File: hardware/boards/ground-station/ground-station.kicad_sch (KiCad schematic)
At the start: 2 parts, among them J101 Raspberry_Pi_2_3, J102 Conn_01x15

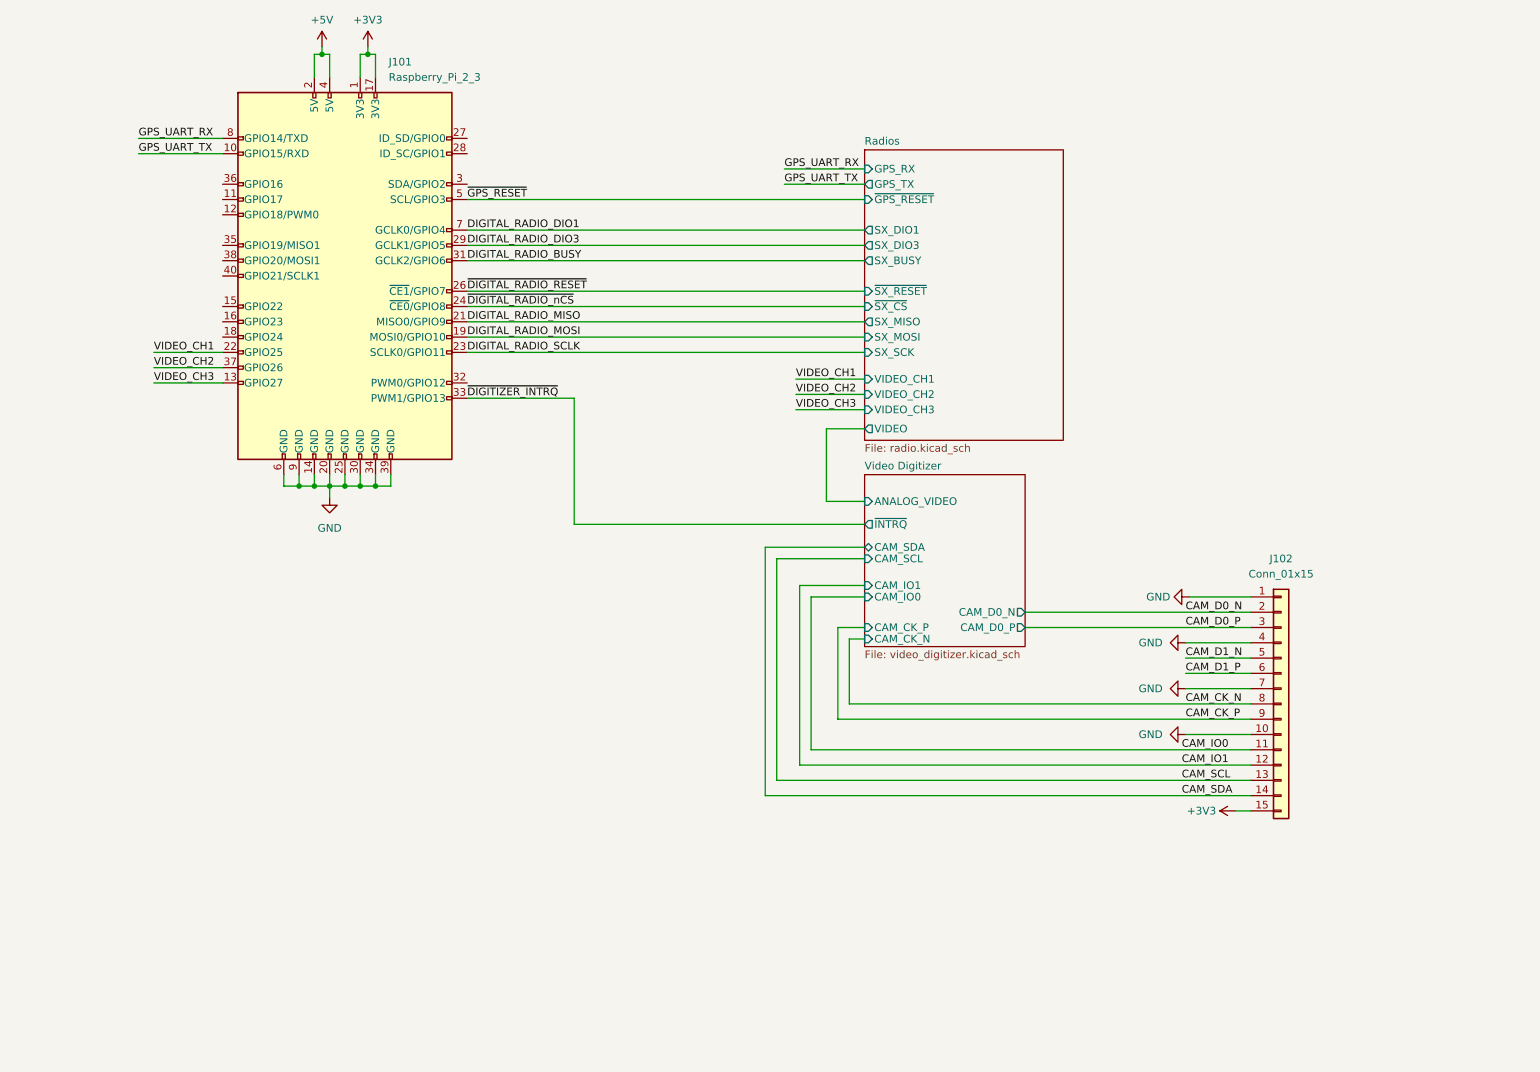
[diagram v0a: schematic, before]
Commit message: Added power supplies to digitizer IC
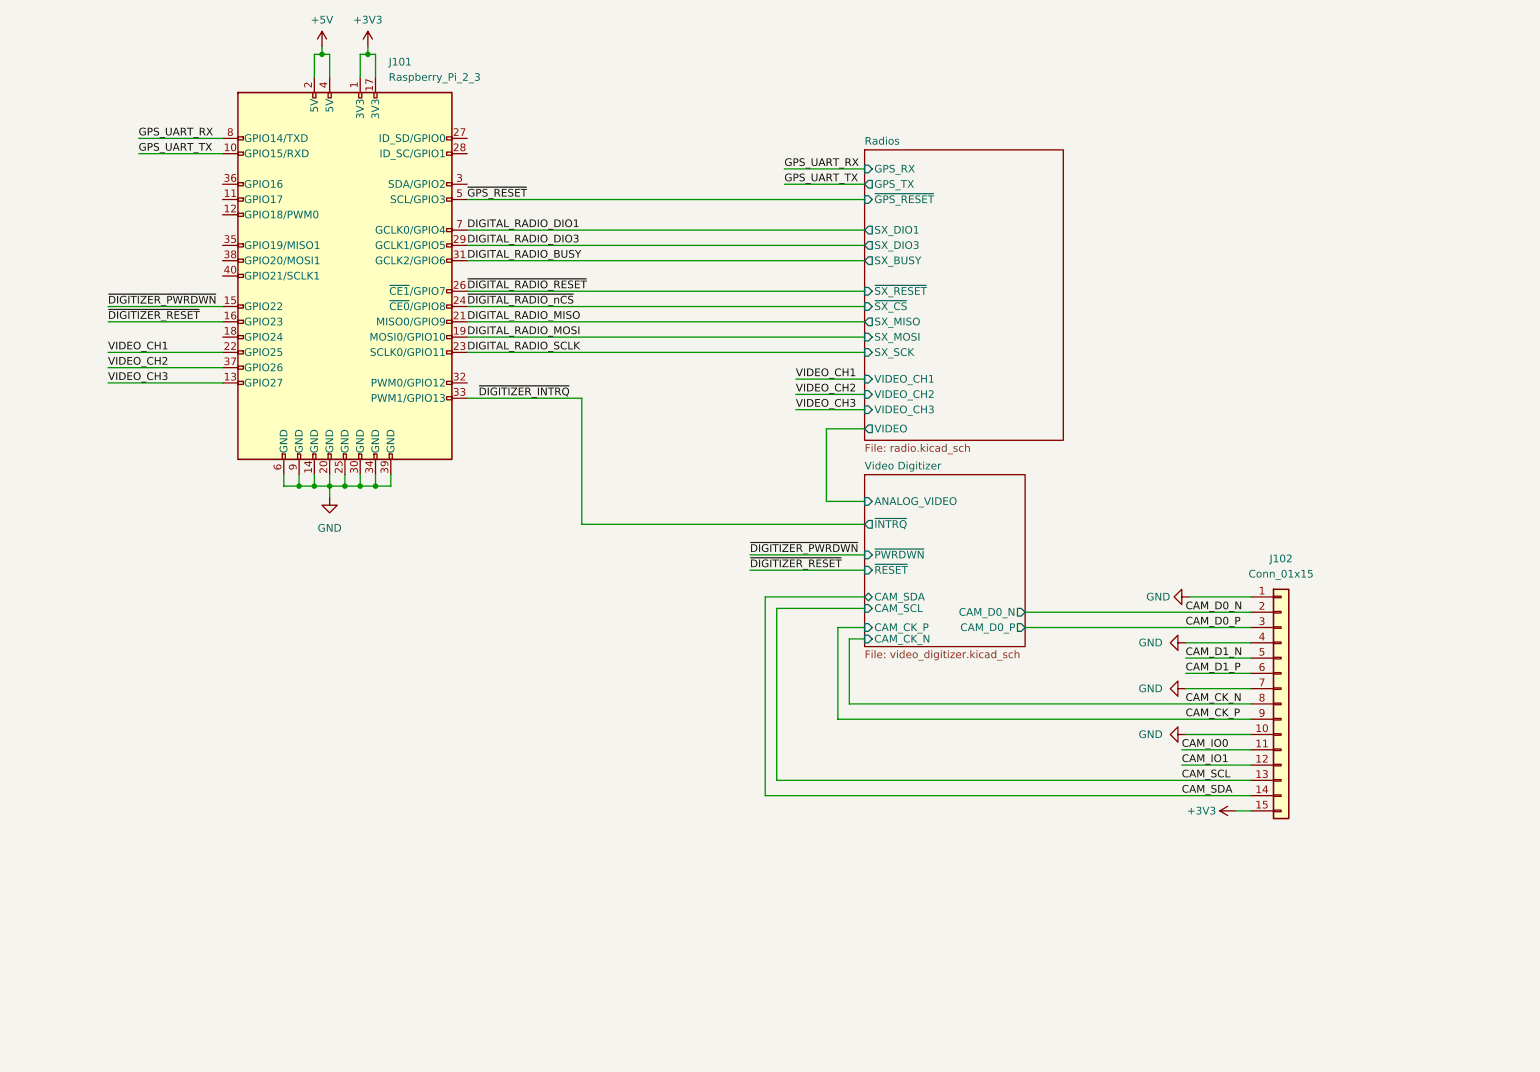
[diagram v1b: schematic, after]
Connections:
- net ~{DIGITIZER_PWRDWN}: now reaches J101.15 (GPIO22)
- net ~{DIGITIZER_RESET}: now reaches J101.16 (GPIO23)
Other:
- sheet Video Digitizer ports: added ~{PWRDWN}, ~{RESET}; removed CAM_IO0, CAM_IO1
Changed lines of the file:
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@@
+    (stroke (width 0) (type default))
+  )
+  (wire (pts (xy 223.52 135.255) (xy 234.95 135.255))
     (stroke (width 0) (type default))
   )
@@
     (stroke (width 0) (type default))
   )
+  (wire (pts (xy 45.085 64.135) (xy 64.135 64.135))
+    (stroke (width 0) (type default))
+  )
+  (wire (pts (xy 45.085 74.295) (xy 64.135 74.295))
+    (stroke (width 0) (type default))
+  )
   (wire (pts (xy 76.835 89.535) (xy 76.835 91.44))
     (stroke (width 0) (type default))
@@
     (stroke (width 0) (type default))
   )
-  (wire (pts (xy 52.705 71.755) (xy 64.135 71.755))
+  (wire (pts (xy 45.085 69.215) (xy 64.135 69.215))
     (stroke (width 0) (type default))
   )
@@
     (stroke (width 0) (type default))
   )
-  (wire (pts (xy 160.02 137.795) (xy 234.95 137.795))
-    (stroke (width 0) (type default))
-  )
   (wire (pts (xy 79.375 23.495) (xy 79.375 19.685))
     (stroke (width 0) (type default))
@@
     (stroke (width 0) (type default))
   )
-  (wire (pts (xy 122.555 97.79) (xy 122.555 76.835))
-    (stroke (width 0) (type default))
-  )
-  (wire (pts (xy 161.925 109.855) (xy 161.925 135.255))
+  (wire (pts (xy 123.825 97.79) (xy 123.825 76.835))
     (stroke (width 0) (type default))
   )
@@
     (stroke (width 0) (type default))
   )
-  (wire (pts (xy 170.815 103.505) (xy 156.21 103.505))
+  (wire (pts (xy 170.815 111.76) (xy 156.21 111.76))
     (stroke (width 0) (type default))
   )
@@
     (stroke (width 0) (type default))
   )
-  (wire (pts (xy 170.815 109.855) (xy 161.925 109.855))
-    (stroke (width 0) (type default))
-  )
-  (wire (pts (xy 161.925 135.255) (xy 234.95 135.255))
+  (wire (pts (xy 45.085 71.755) (xy 64.135 71.755))
+    (stroke (width 0) (type default))
+  )
+  (wire (pts (xy 45.085 61.595) (xy 64.135 61.595))
     (stroke (width 0) (type default))
   )
@@
     (stroke (width 0) (type default))
   )
-  (wire (pts (xy 52.705 74.295) (xy 64.135 74.295))
+  (wire (pts (xy 223.52 137.795) (xy 234.95 137.795))
     (stroke (width 0) (type default))
   )
@@
     (stroke (width 0) (type default))
   )
-  (wire (pts (xy 160.02 107.95) (xy 160.02 137.795))
-    (stroke (width 0) (type default))
-  )
   (wire (pts (xy 89.535 19.685) (xy 88.265 19.685))
     (stroke (width 0) (type default))
@@
     (stroke (width 0) (type default))
   )
+  (wire (pts (xy 151.765 105.41) (xy 170.815 105.41))
+    (stroke (width 0) (type default))
+  )
   (wire (pts (xy 84.455 91.44) (xy 81.915 91.44))
     (stroke (width 0) (type default))
@@
     (stroke (width 0) (type default))
   )
-  (wire (pts (xy 122.555 76.835) (xy 104.775 76.835))
+  (wire (pts (xy 104.775 76.835) (xy 123.825 76.835))
     (stroke (width 0) (type default))
   )
@@
     (stroke (width 0) (type default))
   )
-  (wire (pts (xy 156.21 103.505) (xy 156.21 140.335))
-    (stroke (width 0) (type default))
-  )
-  (wire (pts (xy 170.815 101.6) (xy 154.305 101.6))
+  (wire (pts (xy 156.21 111.76) (xy 156.21 140.335))
+    (stroke (width 0) (type default))
+  )
+  (wire (pts (xy 170.815 109.855) (xy 154.305 109.855))
     (stroke (width 0) (type default))
   )
@@
     (stroke (width 0) (type default))
   )
-  (wire (pts (xy 154.305 101.6) (xy 154.305 142.875))
-    (stroke (width 0) (type default))
-  )
-  (wire (pts (xy 170.815 107.95) (xy 160.02 107.95))
+  (wire (pts (xy 154.305 109.855) (xy 154.305 142.875))
     (stroke (width 0) (type default))
   )
@@
     (stroke (width 0) (type default))
   )
-  (wire (pts (xy 170.815 97.79) (xy 122.555 97.79))
-    (stroke (width 0) (type default))
-  )
-  (wire (pts (xy 52.705 69.215) (xy 64.135 69.215))
+  (wire (pts (xy 170.815 97.79) (xy 123.825 97.79))
     (stroke (width 0) (type default))
   )
@@
     (stroke (width 0) (type default))
   )
+  (wire (pts (xy 151.765 102.87) (xy 170.815 102.87))
+    (stroke (width 0) (type default))
+  )
   (wire (pts (xy 104.775 69.215) (xy 170.815 69.215))
     (stroke (width 0) (type default))
@@
     (effects (font (size 1.27 1.27)) (justify left bottom))
   )
-  (label "VIDEO_CH3" (at 52.705 74.295 0) (fields_autoplaced)
+  (label "VIDEO_CH3" (at 45.085 74.295 0) (fields_autoplaced)
+    (effects (font (size 1.27 1.27)) (justify left bottom))
+  )
+  (label "~{DIGITIZER_PWRDWN}" (at 151.765 102.87 0) (fields_autoplaced)
     (effects (font (size 1.27 1.27)) (justify left bottom))
   )
@@
     (effects (font (size 1.27 1.27)) (justify left bottom))
   )
-  (label "VIDEO_CH2" (at 52.705 71.755 0) (fields_autoplaced)
+  (label "VIDEO_CH2" (at 45.085 71.755 0) (fields_autoplaced)
+    (effects (font (size 1.27 1.27)) (justify left bottom))
+  )
+  (label "~{DIGITIZER_RESET}" (at 45.085 64.135 0) (fields_autoplaced)
     (effects (font (size 1.27 1.27)) (justify left bottom))
   )
@@
     (effects (font (size 1.27 1.27)) (justify left bottom))
   )
-  (label "VIDEO_CH1" (at 52.705 69.215 0) (fields_autoplaced)
+  (label "VIDEO_CH1" (at 45.085 69.215 0) (fields_autoplaced)
     (effects (font (size 1.27 1.27)) (justify left bottom))
   )
@@
     (effects (font (size 1.27 1.27)) (justify left bottom))
   )
+  (label "~{DIGITIZER_PWRDWN}" (at 45.085 61.595 0) (fields_autoplaced)
+    (effects (font (size 1.27 1.27)) (justify left bottom))
+  )
   (label "CAM_SCL" (at 223.52 140.335 0) (fields_autoplaced)
     (effects (font (size 1.27 1.27)) (justify left bottom))
@@
     (effects (font (size 1.27 1.27)) (justify left bottom))
   )
-  (label "~{DIGITIZER_INTRQ}" (at 104.775 76.835 0) (fields_autoplaced)
+  (label "~{DIGITIZER_INTRQ}" (at 106.68 76.835 0) (fields_autoplaced)
     (effects (font (size 1.27 1.27)) (justify left bottom))
   )
@@
   )
   (label "CAM_D1_N" (at 224.155 120.015 0) (fields_autoplaced)
+    (effects (font (size 1.27 1.27)) (justify left bottom))
+  )
+  (label "~{DIGITIZER_RESET}" (at 151.765 105.41 0) (fields_autoplaced)
     (effects (font (size 1.27 1.27)) (justify left bottom))
   )
@@
       (effects (font (size 1.27 1.27)) (justify left))
     )
-    (pin "CAM_IO0" input (at 170.815 109.855 180)
-      (effects (font (size 1.27 1.27)) (justify left))
-    )
-    (pin "CAM_IO1" input (at 170.815 107.95 180)
-      (effects (font (size 1.27 1.27)) (justify left))
-    )
-    (pin "CAM_SCL" input (at 170.815 103.505 180)
-      (effects (font (size 1.27 1.27)) (justify left))
-    )
-    (pin "CAM_SDA" bidirectional (at 170.815 101.6 180)
+    (pin "CAM_SCL" input (at 170.815 111.76 180)
+      (effects (font (size 1.27 1.27)) (justify left))
+    )
+    (pin "CAM_SDA" bidirectional (at 170.815 109.855 180)
       (effects (font (size 1.27 1.27)) (justify left))
     )
@@
       (effects (font (size 1.27 1.27)) (justify left))
     )
+    (pin "~{PWRDWN}" input (at 170.815 102.87 180)
+      (effects (font (size 1.27 1.27)) (justify left))
+    )
+    (pin "~{RESET}" input (at 170.815 105.41 180)
+      (effects (font (size 1.27 1.27)) (justify left))
+    )

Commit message: transmitter tx stuff
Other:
- added sheet Power (Power.kicad_sch)
- added sheet Wireless Power TX (WirelessPowerTX.kicad_sch)
- note added: "NEED THESE I2C PINS MOVE IO SOMEWHERE"
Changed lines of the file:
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@@
     (stroke (width 0) (type default))
+  )
+  (text "NEED THESE I2C PINS\nMOVE IO SOMEWHERE\n" (at 116.84 40.64 0)
+    (effects (font (size 1.27 1.27)) (justify left bottom))
   )
   (label "CAM_D0_N" (at 224.155 112.395 0) (fields_autoplaced)
@@
     )
   )
+  (sheet (at 101.6 146.05) (size 46.99 38.1) (fields_autoplaced)
+    (stroke (width 0.1524) (type solid))
+    (fill (color 0 0 0 0.0000))
+    (property "Sheetname" "Wireless Power TX" (at 101.6 145.3384 0)
+      (effects (font (size 1.27 1.27)) (justify left bottom))
+    )
+    (property "Sheetfile" "WirelessPowerTX.kicad_sch" (at 101.6 184.7346 0)
+      (effects (font (size 1.27 1.27)) (justify left top))
+    )
+    (instances
+      (project "ground-station"
+        (path "/ce329892-de08-4d39-b253-15f3aaf1c085" (page "7"))
+      )
+    )
+  )
   (sheet (at 170.815 35.56) (size 33.02 48.26) (fields_autoplaced)
     (stroke (width 0.1524) (type solid))
@@
       )
     )
+  )
+  (sheet (at 29.21 102.87) (size 39.37 35.56) (fields_autoplaced)
+    (stroke (width 0.1524) (type solid))
+    (fill (color 0 0 0 0.0000))
+    (property "Sheetname" "Power" (at 29.21 102.1584 0)
+      (effects (font (size 1.27 1.27)) (justify left bottom))
+    )
+    (property "Sheetfile" "Power.kicad_sch" (at 29.21 139.0146 0)
+      (effects (font (size 1.27 1.27)) (justify left top))
+    )
+    (instances
+      (project "ground-station"
+        (path "/ce329892-de08-4d39-b253-15f3aaf1c085" (page "8"))
+      )
+    )

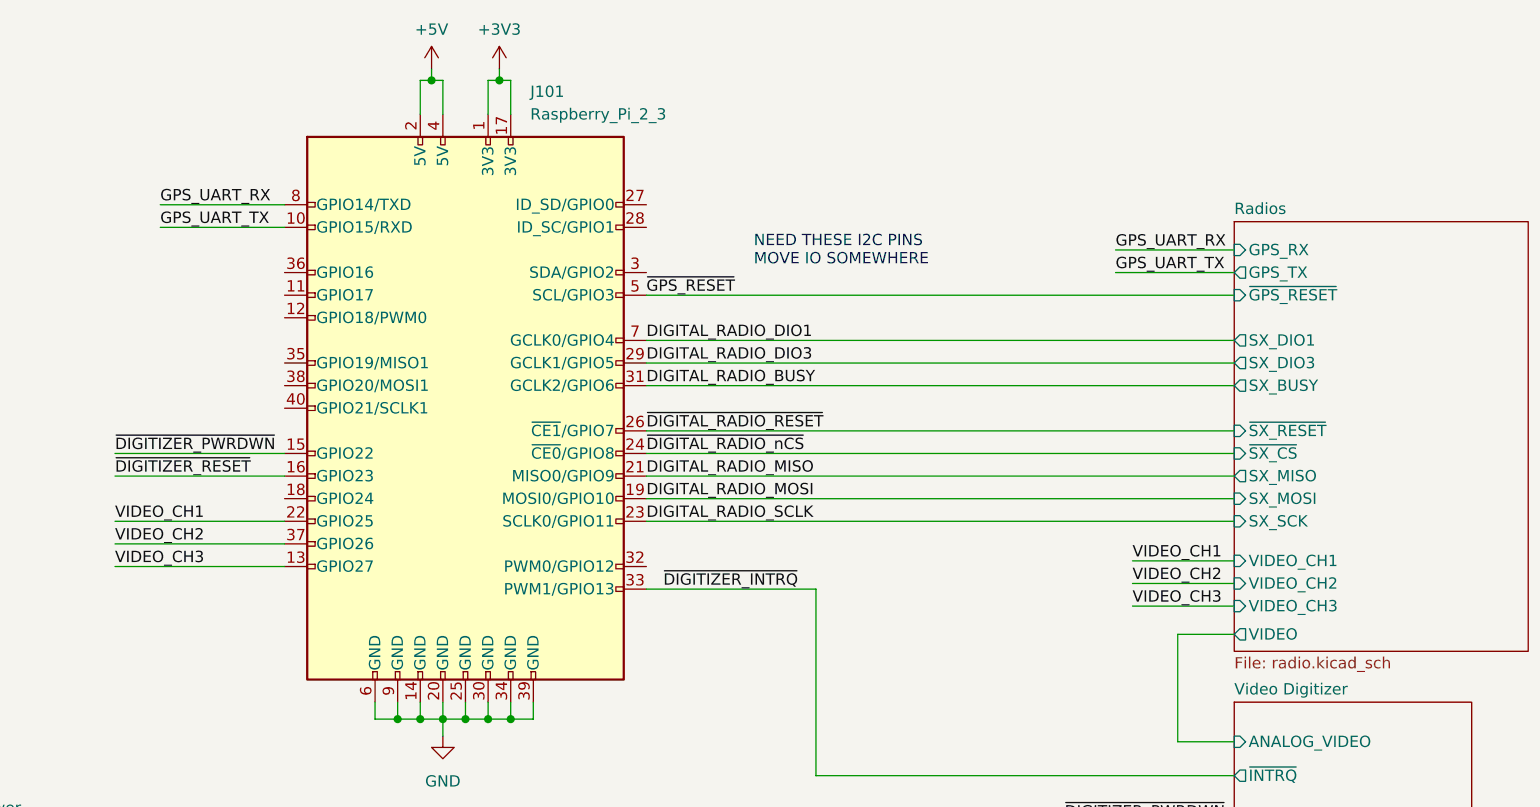
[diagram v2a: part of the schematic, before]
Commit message: Updated video radio to RX5808
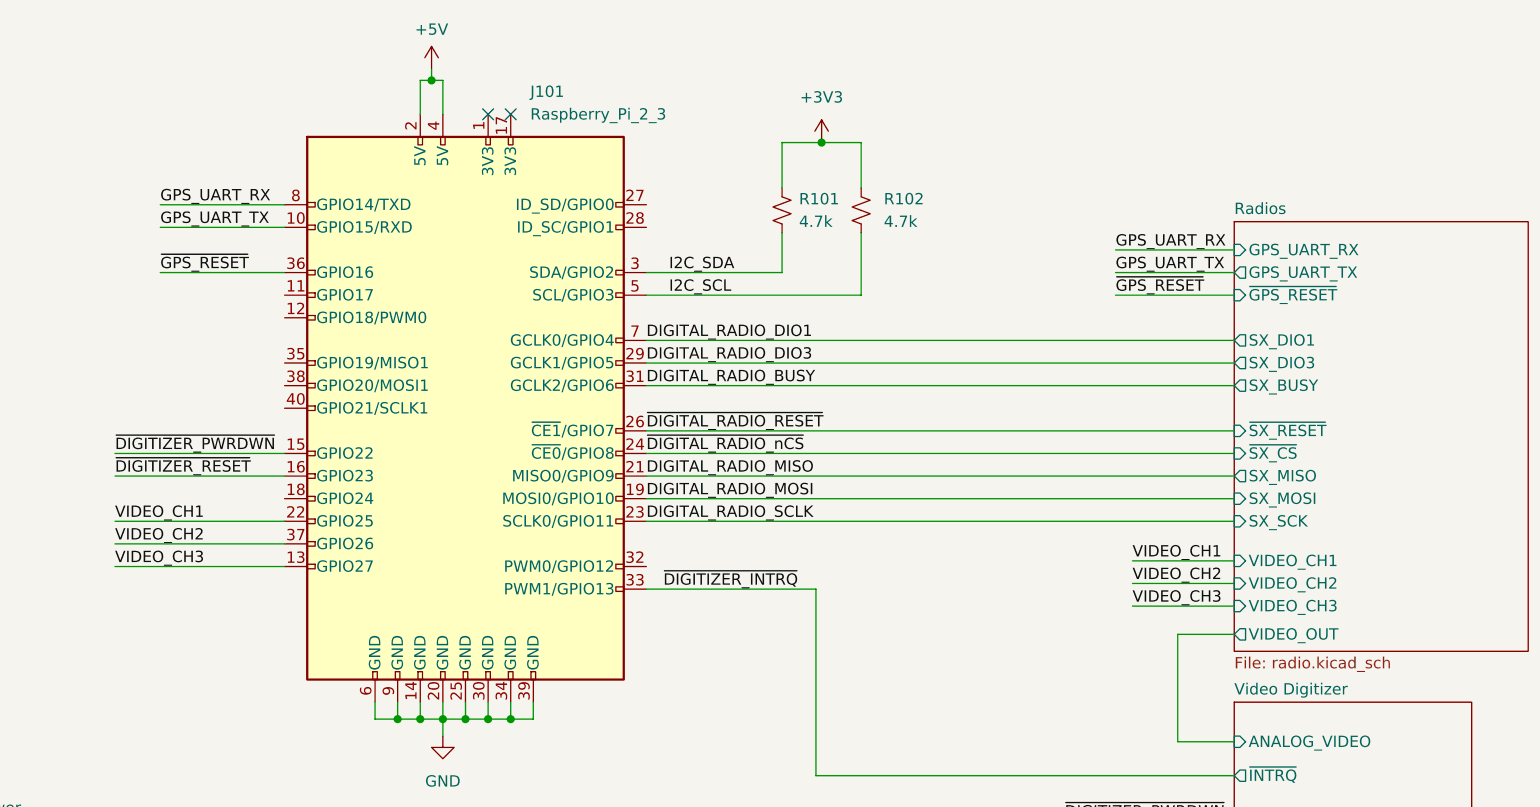
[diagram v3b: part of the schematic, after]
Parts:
- added R101, R102: 4.7k, symbol Device:R_Small_US
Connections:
- net +3V3: now also R101.2, R102.2; no longer J101.1 (3V3), J101.17 (3V3)
- net ~{GPS_RESET}: now also J101.36 (GPIO16); no longer J101.5 (SCL/GPIO3)
- net I2C_SDA: now reaches J101.3 (SDA/GPIO2)
- net I2C_SDA: now also R101.1
- new net I2C_SCL: J101.5 (SCL/GPIO3), R102.1
- no-connect marks 0 -> 2
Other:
- sheet Radios ports: added GPS_UART_RX, GPS_UART_TX, VIDEO_OUT; removed GPS_RX, GPS_TX, VIDEO
- note removed: "NEED THESE I2C PINS MOVE IO SOMEWHERE"

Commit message: sch review
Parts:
- added J5: Conn_01x12, symbol Connector_Generic:Conn_01x12
- added R23, R24, R25, R26: 0, symbol Device:R_Small
- added R3: 0, Resistor_SMD:R_1206_3216Metric, symbol Device:R_Small
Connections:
- net +3V3: now also J5.2 (Pin_2)
- net +5V: now also J5.1 (Pin_1), R3.1; no longer J101.2 (5V), J101.4 (5V)
- net CAM_D0_N: now also R25.1; no longer J102.2 (Pin_2)
- net CAM_D0_P: now also R26.1; no longer J102.3 (Pin_3)
- net CAM_D1_N: now also R23.1; no longer J102.5 (Pin_5)
- net CAM_D1_P: now also R24.1; no longer J102.6 (Pin_6)
- net DIGITAL_RADIO_BUSY: now also J5.5 (Pin_5)
- net DIGITAL_RADIO_DIO1: now also J5.3 (Pin_3)
- net DIGITAL_RADIO_DIO3: now also J5.4 (Pin_4)
- net DIGITAL_RADIO_MISO: now also J5.8 (Pin_8)
- net DIGITAL_RADIO_MOSI: now also J5.9 (Pin_9)
- net DIGITAL_RADIO_SCLK: now also J5.10 (Pin_10)
- net GND: now also J5.11 (Pin_11), J5.12 (Pin_12)
- net ~{DIGITAL_RADIO_RESET}: now also J5.6 (Pin_6)
- net ~{DIGITAL_RADIO_nCS}: now also J5.7 (Pin_7)
- new net: J101.2 (5V), J101.4 (5V), R3.2
- new net CAM_D0_CONN_N: J102.2 (Pin_2), R25.2
- new net CAM_D0_CONN_P: J102.3 (Pin_3), R26.2
- new net CAM_D1_CONN_N: J102.5 (Pin_5), R23.2
- new net CAM_D1_CONN_P: J102.6 (Pin_6), R24.2
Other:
- removed sheet Wireless Power TX
- moved on the sheet: J102
